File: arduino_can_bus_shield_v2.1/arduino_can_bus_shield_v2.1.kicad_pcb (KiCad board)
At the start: 2 copper layers, 61.1 x 53.3 mm, 37 parts, among them J1 Power, J2 Digital/PWM, J3 Analog, J4 Digital/PWM, J6 xt60 male, J7 molex_3.0, M1 MPU9250_module, SW1 User, SW2 User, SW3 SW_DIP_x04, U1 MP1584, U2 MCP2551-I-SN, U3 MCP2515-xST, Y1 16MHz

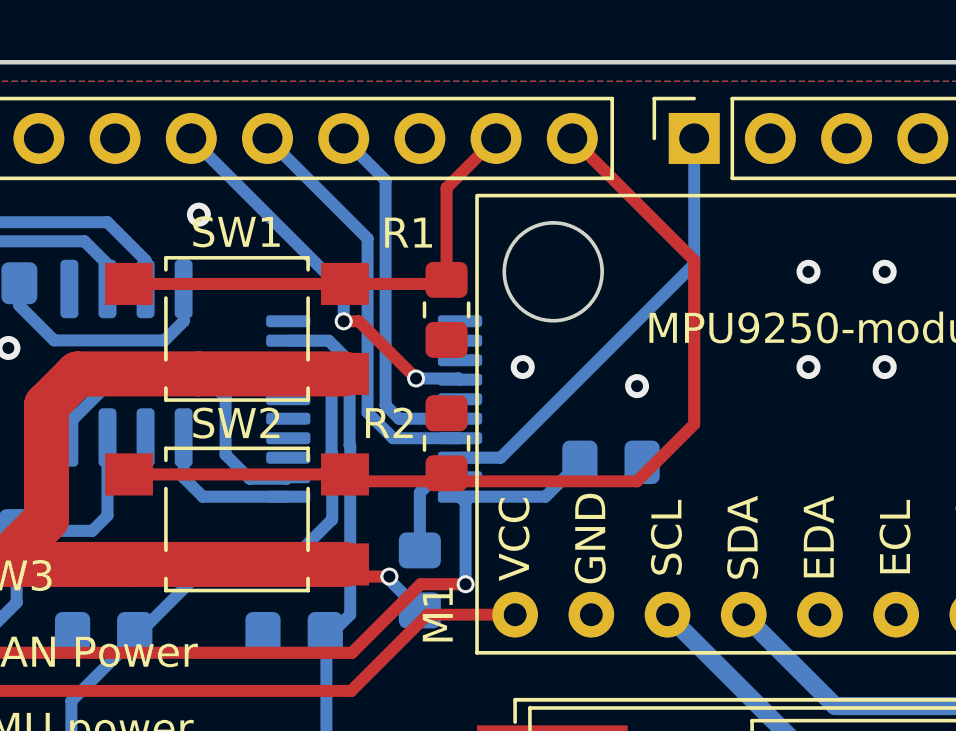
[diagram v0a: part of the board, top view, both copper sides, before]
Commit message: fixed pin 9 button to pin 6
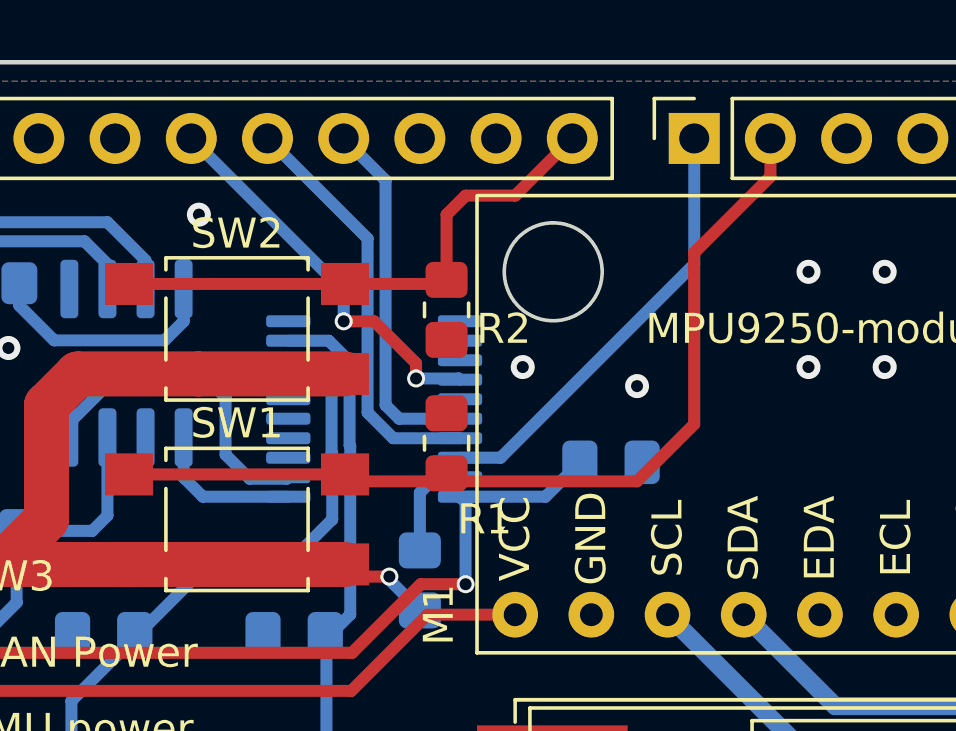
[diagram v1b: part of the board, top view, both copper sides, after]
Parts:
- moved SW1 6.35 mm to (130.5, 61.9)
- moved SW2 6.35 mm to (130.5, 55.5)
- moved R1 4.45 mm to (137.5, 59.4), turned to 90 degrees
- moved R2 4.45 mm to (137.5, 54.9), turned to -90 degrees
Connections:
- R1 pad 1: /9(**) -> /*6
- SW1 pad 1: /9(**) -> /*6
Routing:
- net /*6: track 0.00 -> 30.3 mm
- net /9(**): track 16.0 -> 0.00 mm
- net /8: track 30.9 -> 18.1 mm
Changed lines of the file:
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@@
   )
   (footprint "Resistor_SMD:R_0805_2012Metric_Pad1.20x1.40mm_HandSolder" (layer "F.Cu")
-    (at 137.465 59.36 90)
+    (at 137.465 54.915 -90)
     (descr "Resistor SMD 0805 (2012 Metric), square (rectangular) end terminal, IPC_7351 nominal with elongated pad for handsoldering. (Body size source: IPC-SM-782 page 72, https://www.pcb-3d.com/wordpress/wp-content/uploads/ipc-sm-782a_amendment_1_and_2.pdf), generated with kicad-footprint-generator")
     (tags "resistor handsolder")
@@
     (property "Sheetname" "")
     (attr smd)
-    (fp_text reference "R2" (at 0.635 -1.905 180) (layer "F.SilkS")
+    (fp_text reference "R2" (at 0.635 -1.905) (layer "F.SilkS")
       (effects (font (size 1 1) (thickness 0.15)))
     )
@@
     (fp_line (start 1 0.625) (end -1 0.625) (layer "F.Fab") (width 0.1))
     (fp_line (start 1 -0.625) (end 1 0.625) (layer "F.Fab") (width 0.1))
-    (pad "1" smd roundrect (at -1 0 90) (size 1.2 1.4) (layers "F.Cu" "F.Paste" "F.Mask") (roundrect_rratio 0.2083333333)
+    (pad "1" smd roundrect (at -1 0 270) (size 1.2 1.4) (layers "F.Cu" "F.Paste" "F.Mask") (roundrect_rratio 0.2083333333)
       (net 12 "/8") (pintype "passive"))
-    (pad "2" smd roundrect (at 1 0 90) (size 1.2 1.4) (layers "F.Cu" "F.Paste" "F.Mask") (roundrect_rratio 0.2083333333)
+    (pad "2" smd roundrect (at 1 0 270) (size 1.2 1.4) (layers "F.Cu" "F.Paste" "F.Mask") (roundrect_rratio 0.2083333333)
       (net 1 "GND") (pintype "passive"))
     (model "${KICAD6_3DMODEL_DIR}/Resistor_SMD.3dshapes/R_0805_2012Metric.wrl"
@@
   )
   (footprint "Button_Switch_SMD:SW_SPST_TL3305A" (layer "F.Cu")
-    (at 130.48 55.55)
+    (at 130.48 61.9)
     (descr "https://www.e-switch.com/system/asset/product_line/data_sheet/213/TL3305.pdf")
     (tags "TL3305 Series Tact Switch")
@@
     (fp_circle (center 0 0) (end 1.25 0) (layer "F.Fab") (width 0.1) (fill none))
     (pad "1" smd rect (at 3.6 -1.5) (size 1.6 1.4) (layers "F.Cu" "F.Paste" "F.Mask")
-      (net 43 "/9(**)") (pinfunction "1") (pintype "passive"))
+      (net 17 "/*6") (pinfunction "1") (pintype "passive"))
     (pad "1" smd rect (at -3.6 -1.5) (size 1.6 1.4) (layers "F.Cu" "F.Paste" "F.Mask")
-      (net 43 "/9(**)") (pinfunction "1") (pintype "passive"))
+      (net 17 "/*6") (pinfunction "1") (pintype "passive"))
     (pad "2" smd rect (at 3.6 1.5) (size 1.6 1.4) (layers "F.Cu" "F.Paste" "F.Mask")
       (net 3 "+5V") (pinfunction "2") (pintype "passive"))
@@
   )
   (footprint "Button_Switch_SMD:SW_SPST_TL3305C" (layer "F.Cu")
-    (at 130.48 61.9)
+    (at 130.48 55.55)
     (descr "https://www.e-switch.com/system/asset/product_line/data_sheet/213/TL3305.pdf")
     (tags "TL3305 Series Tact Switch")
@@
   )
   (footprint "Resistor_SMD:R_0805_2012Metric_Pad1.20x1.40mm_HandSolder" (layer "F.Cu")
-    (at 137.465 54.915 -90)
+    (at 137.465 59.36 90)
     (descr "Resistor SMD 0805 (2012 Metric), square (rectangular) end terminal, IPC_7351 nominal with elongated pad for handsoldering. (Body size source: IPC-SM-782 page 72, https://www.pcb-3d.com/wordpress/wp-content/uploads/ipc-sm-782a_amendment_1_and_2.pdf), generated with kicad-footprint-generator")
     (tags "resistor handsolder")
@@
     (property "Sheetname" "")
     (attr smd)
-    (fp_text reference "R1" (at -2.54 1.27 180) (layer "F.SilkS")
+    (fp_text reference "R1" (at -2.54 1.27) (layer "F.SilkS")
       (effects (font (size 1 1) (thickness 0.15)))
     )
@@
     (fp_line (start 1 -0.625) (end 1 0.625) (layer "F.Fab") (width 0.1))
     (fp_line (start 1 0.625) (end -1 0.625) (layer "F.Fab") (width 0.1))
-    (pad "1" smd roundrect (at -1 0 270) (size 1.2 1.4) (layers "F.Cu" "F.Paste" "F.Mask") (roundrect_rratio 0.2083333333)
-      (net 43 "/9(**)") (pintype "passive"))
-    (pad "2" smd roundrect (at 1 0 270) (size 1.2 1.4) (layers "F.Cu" "F.Paste" "F.Mask") (roundrect_rratio 0.2083333333)
+    (pad "1" smd roundrect (at -1 0 90) (size 1.2 1.4) (layers "F.Cu" "F.Paste" "F.Mask") (roundrect_rratio 0.2083333333)
+      (net 17 "/*6") (pintype "passive"))
+    (pad "2" smd roundrect (at 1 0 90) (size 1.2 1.4) (layers "F.Cu" "F.Paste" "F.Mask") (roundrect_rratio 0.2083333333)
       (net 1 "GND") (pintype "passive"))
     (model "${KICAD6_3DMODEL_DIR}/Resistor_SMD.3dshapes/R_0805_2012Metric.wrl"
@@
   (segment (start 163.881 81.081) (end 165.845 83.045) (width 0.6) (layer "B.Cu") (net 10))
   (segment (start 160.452 69.393) (end 163.881 72.822) (width 0.6) (layer "B.Cu") (net 10))
-  (segment (start 145.72 53.264) (end 145.72 58.725) (width 0.4) (layer "F.Cu") (net 12))
-  (segment (start 134.08 60.4) (end 126.88 60.4) (width 0.4) (layer "F.Cu") (net 12))
-  (segment (start 143.815 60.63) (end 134.31 60.63) (width 0.4) (layer "F.Cu") (net 12))
-  (segment (start 141.656 49.2) (end 145.72 53.264) (width 0.4) (layer "F.Cu") (net 12))
-  (segment (start 145.72 58.725) (end 143.815 60.63) (width 0.4) (layer "F.Cu") (net 12))
-  (segment (start 134.31 60.63) (end 134.08 60.4) (width 0.4) (layer "F.Cu") (net 12))
+  (segment (start 137.465 53.915) (end 137.33 54.05) (width 0.4) (layer "F.Cu") (net 12))
+  (segment (start 138.1 51.105) (end 139.751 51.105) (width 0.4) (layer "F.Cu") (net 12))
+  (segment (start 137.33 54.05) (end 134.08 54.05) (width 0.4) (layer "F.Cu") (net 12))
+  (segment (start 139.751 51.105) (end 141.656 49.2) (width 0.4) (layer "F.Cu") (net 12))
+  (segment (start 137.465 53.915) (end 137.465 51.74) (width 0.4) (layer "F.Cu") (net 12))
+  (segment (start 137.465 51.74) (end 138.1 51.105) (width 0.4) (layer "F.Cu") (net 12))
+  (segment (start 134.08 54.05) (end 126.88 54.05) (width 0.4) (layer "F.Cu") (net 12))
   (segment (start 145.72 53.391) (end 139.269 59.842) (width 0.4) (layer "B.Cu") (net 13))
   (segment (start 139.269 59.842) (end 137.9145 59.842) (width 0.4) (layer "B.Cu") (net 13))
   (segment (start 145.72 49.2) (end 145.72 53.391) (width 0.4) (layer "B.Cu") (net 13))
+  (segment (start 134.31 60.63) (end 143.815 60.63) (width 0.4) (layer "F.Cu") (net 17))
+  (segment (start 145.72 58.725) (end 145.72 53.01) (width 0.4) (layer "F.Cu") (net 17))
+  (segment (start 145.72 53.01) (end 148.26 50.47) (width 0.4) (layer "F.Cu") (net 17))
+  (segment (start 134.08 60.4) (end 126.88 60.4) (width 0.4) (layer "F.Cu") (net 17))
+  (segment (start 143.815 60.63) (end 145.72 58.725) (width 0.4) (layer "F.Cu") (net 17))
+  (segment (start 134.08 60.4) (end 134.31 60.63) (width 0.4) (layer "F.Cu") (net 17))
+  (segment (start 148.26 50.47) (end 148.26 49.2) (width 0.4) (layer "F.Cu") (net 17))
   (segment (start 164.135 82.855) (end 164.135 82.215) (width 0.6) (layer "F.Cu") (net 22))
   (segment (start 164.135 82.215) (end 165.845 80.505) (width 0.6) (layer "F.Cu") (net 22))
@@
   (segment (start 120.574 67.615) (end 134.29 67.615) (width 0.4) (layer "F.Cu") (net 37))
   (segment (start 136.83 65.075) (end 139.751 65.075) (width 0.4) (layer "F.Cu") (net 37))
-  (segment (start 137.465 53.915) (end 137.33 54.05) (width 0.4) (layer "F.Cu") (net 43))
-  (segment (start 137.33 54.05) (end 134.08 54.05) (width 0.4) (layer "F.Cu") (net 43))
-  (segment (start 137.465 50.851) (end 137.465 53.915) (width 0.4) (layer "F.Cu") (net 43))
-  (segment (start 139.116 49.2) (end 137.465 50.851) (width 0.4) (layer "F.Cu") (net 43))
-  (segment (start 134.08 54.05) (end 126.88 54.05) (width 0.4) (layer "F.Cu") (net 43))
   (segment (start 123.225 54.772) (end 123.225 54.026) (width 0.4) (layer "B.Cu") (net 44))
   (segment (start 128.702 54.218) (end 128.702 55.296) (width 0.4) (layer "B.Cu") (net 44))
@@
   (segment (start 132.1395 60.542) (end 132.1895 60.492) (width 0.4) (layer "B.Cu") (net 48))
   (segment (start 124.892 59.168) (end 124.892 58.685183) (width 0.4) (layer "B.Cu") (net 48))
-  (segment (start 134.544 55.296) (end 136.449 57.201) (width 0.4) (layer "F.Cu") (net 58))
-  (segment (start 134.036 55.296) (end 134.544 55.296) (width 0.4) (layer "F.Cu") (net 58))
+  (segment (start 136.449 56.693) (end 136.449 57.201) (width 0.4) (layer "F.Cu") (net 58))
+  (segment (start 134.036 55.296) (end 135.052 55.296) (width 0.4) (layer "F.Cu") (net 58))
+  (segment (start 135.052 55.296) (end 136.449 56.693) (width 0.4) (layer "F.Cu") (net 58))
   (via (at 136.449 57.201) (size 0.6) (drill 0.4) (layers "F.Cu" "B.Cu") (net 58))
   (via (at 134.036 55.296) (size 0.6) (drill 0.4) (layers "F.Cu" "B.Cu") (net 58))
